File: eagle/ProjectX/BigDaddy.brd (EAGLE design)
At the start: 100 x 100 mm, 180 parts, among them U10 TC4427AEOA, U11 TC4427AEOA, U12 TC4427AEOA, U13 TC4427AEOA, U19 TC4427AEOA, U20 TC4427AEOA, U21 TC4427AEOA, U22 TC4427AEOA, U23 TC4427AEOA, U24 TC4427AEOA, U25 TC4427AEOA, U26 TC4427AEOA, U27 TC4427AEOA, U28 TC4427AEOA, U29 TC4427AEOA, U3 TC4427AEOA, U30 TC4427AEOA, U31 TC4427AEOA, U32 TC4427AEOA, U34 TC4427AEOA, U35 TC4427AEOA, U36 TC4427AEOA, U37 TC4427AEOA, U38 TC4427AEOA, U39 TC4427AEOA, U4 TC4427AEOA, U40 TC4427AEOA, U41 TC4427AEOA, U42 TC4427AEOA, U43 TC4427AEOA, U44 TC4427AEOA, U45 TC4427AEOA, U5 TC4427AEOA, U55 TC4427AEOA, U56 TC4427AEOA, U57 TC4427AEOA, U58 TC4427AEOA, U59 TC4427AEOA, U60 TC4427AEOA, U61 TC4427AEOA, U62 TC4427AEOA, U63 TC4427AEOA, U7 TC4427AEOA, U9 TC4427AEOA

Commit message: Still routing traces
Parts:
- J1: value (none) -> +20V
- J2: value (none) -> Data
- moved C19 0.25 mm to (7.25, 55.0)
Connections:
- net 23: now also DIP1.152
- net 24: now also DIP1.160
- net 25: now also DIP1.150
- net 30: now also DIP1.153
- net 31: now also DIP1.151
- net 34: now also DIP1.146
- net 39: now also DIP1.145
- net 40: now also DIP1.147
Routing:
- net 83: track 0.00 -> 47.1 mm
- net 82: track 0.00 -> 42.7 mm
- net 74: track 0.00 -> 41.0 mm
- net 73: track 0.00 -> 36.5 mm
- net 65: track 0.00 -> 35.2 mm
- net 64: track 0.00 -> 30.7 mm
- net 34: track 0.00 -> 30.0 mm, vias 0 -> 2
- net 56: track 0.00 -> 28.1 mm
- net 25: track 0.00 -> 27.2 mm, vias 0 -> 2
- net 30: track 0.00 -> 24.1 mm
- net 55: track 0.00 -> 23.5 mm
- net 31: track 0.00 -> 20.1 mm
- net 38: track 0.00 -> 19.9 mm
- net 47: track 0.00 -> 19.8 mm, vias 0 -> 2
- net 46: track 0.00 -> 16.8 mm, vias 0 -> 2
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
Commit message: About 80% complete routing
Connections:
- net 32: now also DIP1.139
- net 33: now also DIP1.144
- net 39: now also DIP1.147; no longer DIP1.145
- net 40: now also DIP1.145; no longer DIP1.147
- net 48: now also DIP1.140
- net 49: now also DIP1.138
- net 57: now also DIP1.135
- net 58: now also DIP1.133
- net 66: now also DIP1.129
- net 67: now also DIP1.127
- net 75: now also DIP1.123
- net 76: now also DIP1.120
- net 84: now also DIP1.116
- net 85: now also DIP1.113
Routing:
- net 84: track 0.00 -> 57.1 mm, vias 0 -> 2
- net 85: track 0.00 -> 54.1 mm, vias 0 -> 2
- net 75: track 0.00 -> 51.1 mm, vias 0 -> 2
- net 76: track 0.00 -> 48.1 mm, vias 0 -> 2
- net 66: track 0.00 -> 47.1 mm, vias 0 -> 2
- net 67: track 0.00 -> 44.2 mm, vias 0 -> 2
- net 57: track 0.00 -> 41.1 mm, vias 0 -> 2
- net 58: track 0.00 -> 38.1 mm, vias 0 -> 2
- net 48: track 0.00 -> 35.5 mm, vias 0 -> 2
- net 49: track 0.00 -> 32.4 mm, vias 0 -> 2
- net 39: track 0.00 -> 30.0 mm, vias 0 -> 2
- net 40: track 0.00 -> 26.8 mm, vias 0 -> 2
- net 33: track 0.00 -> 16.5 mm, vias 0 -> 2
- net 32: track 0.00 -> 12.1 mm, vias 0 -> 2
- net 34: track 30.0 -> 26.0 mm
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
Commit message: More work on routing
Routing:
- net 39: track 30.0 -> 29.2 mm

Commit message: Nearly done!
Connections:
- net 41: now also DIP1.122
- net 42: now also DIP1.126
- net 43: now also DIP1.119
- net 50: now also DIP1.108
- net 51: now also DIP1.112
- net 52: now also DIP1.115
- net 59: now also DIP1.100
- net 60: now also DIP1.106
- net 61: now also DIP1.98
- net 68: now also DIP1.90
- net 69: now also DIP1.93
- net 70: now also DIP1.96
- net 77: now also DIP1.97
- net 78: now also DIP1.94
- net 79: now also DIP1.99
- net 86: now also DIP1.109
- net 87: now also DIP1.107
- net 88: now also DIP1.102

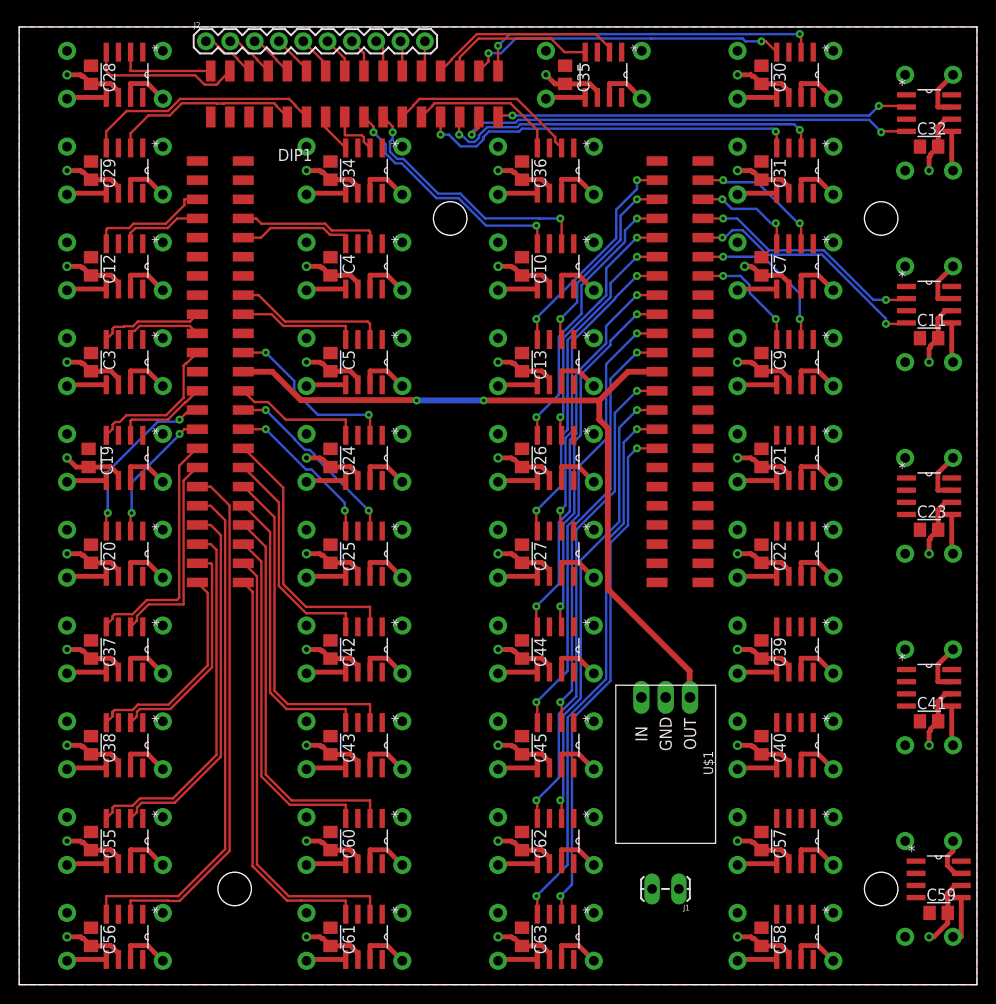
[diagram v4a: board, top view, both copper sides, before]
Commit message: Minor revision to add ground to the data port
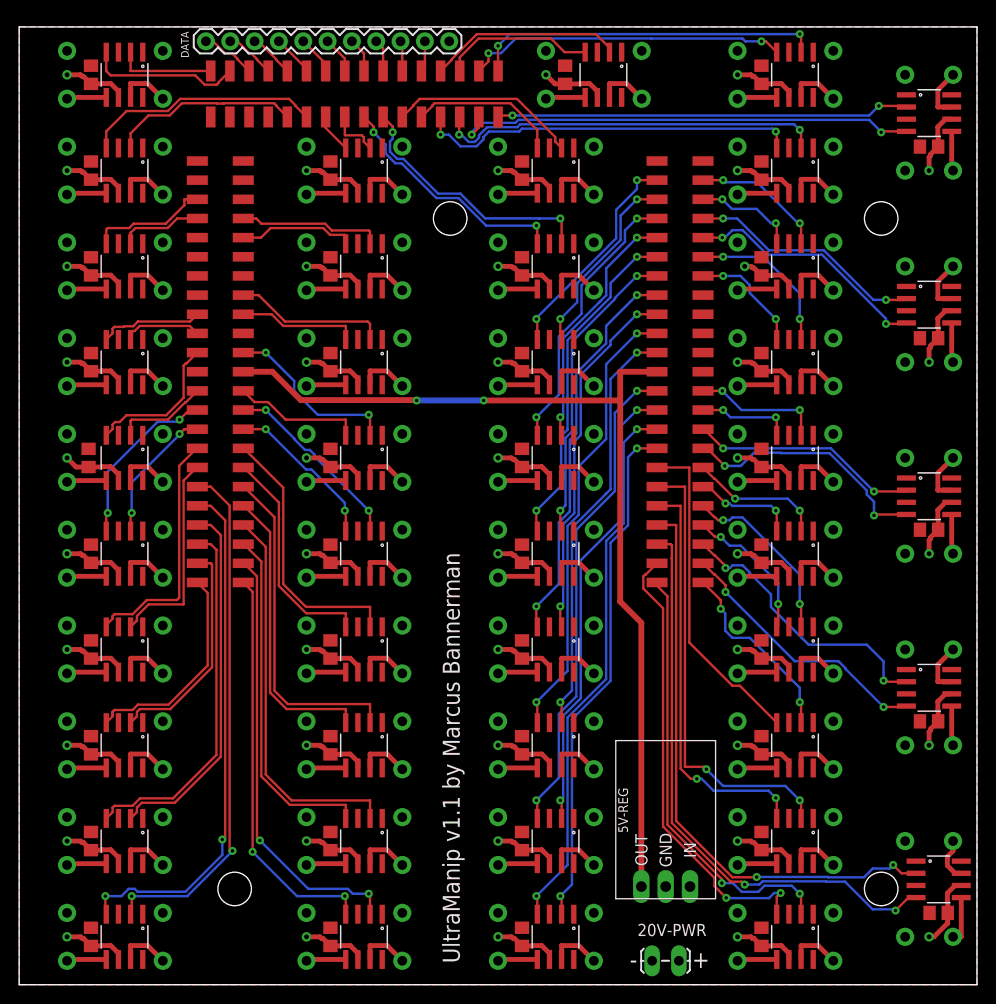
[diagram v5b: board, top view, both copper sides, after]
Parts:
- removed J1: +20V, SparkFun-Connectors:1X02_LOCK_LONGPADS
- removed J2: Data, SparkFun-Connectors:1X10
- removed U$1: OKI-78SR, Parts:OKI-78SR-HORIZ
- added 20V-PWR: +20V, SparkFun-Connectors:1X02_LOCK_LONGPADS
- added 5V-REG: OKI-78SR, Parts:OKI-78SR-HORIZ
- added DATA: Data, SparkFun-Connectors:1X11
- C10, C11, C12, C13, C19, C20, C21, C22, C23, C24, C25, C26, C27, C28, C29, C3, C30, C31, C32, C34, C35, C36, C37, C38, C39, C4, C40, C41, C42, C43, C44, C45, C5, C55, C56, C57, C58, C59, C60, C61, C62, C63, C7, C9: value (none) -> 100nF
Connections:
- net +5V: now also 5V-REG.OUT; no longer U$1.OUT
- net 68: now also DIP1.109; no longer DIP1.90
- net 77: now also DIP1.102; no longer DIP1.97
- net 78: now also DIP1.107; no longer DIP1.94
- net 86: now also DIP1.94; no longer DIP1.109
- net 87: now also DIP1.90; no longer DIP1.107
- net 88: now also DIP1.97; no longer DIP1.102
- net GND: now also 20V-PWR.2, 5V-REG.GND, DATA.11; no longer J1.2, U$1.GND
- net N$1: now also DATA.1; no longer J2.1
- net N$13: now also DATA.5; no longer J2.5
- net N$14: now also DATA.6; no longer J2.6
- net N$17: now also DATA.7; no longer J2.7
- net N$18: now also DATA.8; no longer J2.8
- net N$2: now also DATA.2; no longer J2.2
- net N$29: now also DATA.9; no longer J2.9
- net N$3: now also DATA.3; no longer J2.3
- net N$30: now also DATA.10; no longer J2.10
- net N$4: now also DATA.4; no longer J2.4
- net VDD: now also 20V-PWR.1, 5V-REG.IN; no longer J1.1, U$1.IN
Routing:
- net 79: track 0.00 -> 61.3 mm, vias 0 -> 2
- net 88: track 0.00 -> 60.7 mm, vias 0 -> 2
- net 78: track 0.00 -> 47.6 mm, vias 0 -> 2
- net 86: track 0.00 -> 47.4 mm, vias 0 -> 2
- net 87: track 0.00 -> 45.5 mm, vias 0 -> 2
- net 77: track 0.00 -> 43.3 mm, vias 0 -> 2
- net 68: track 0.00 -> 34.2 mm
- net 61: track 0.00 -> 29.5 mm, vias 0 -> 2
- net 70: track 0.00 -> 27.9 mm, vias 0 -> 2
- net 52: track 0.00 -> 26.6 mm, vias 0 -> 2
- net 43: track 0.00 -> 24.1 mm, vias 0 -> 2
- net 69: track 0.00 -> 19.9 mm, vias 0 -> 2
- net 60: track 0.00 -> 18.9 mm, vias 0 -> 2
- net +5V: track 80.6 -> 99.1 mm
- net 59: track 0.00 -> 15.0 mm, vias 0 -> 2
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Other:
- board text added: "+"
- board text added: "-"
- board text added: "UltraManip v1.1 by Marcus Bannerman"

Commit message: Slight improvements to the board, incase we need a new version in the future
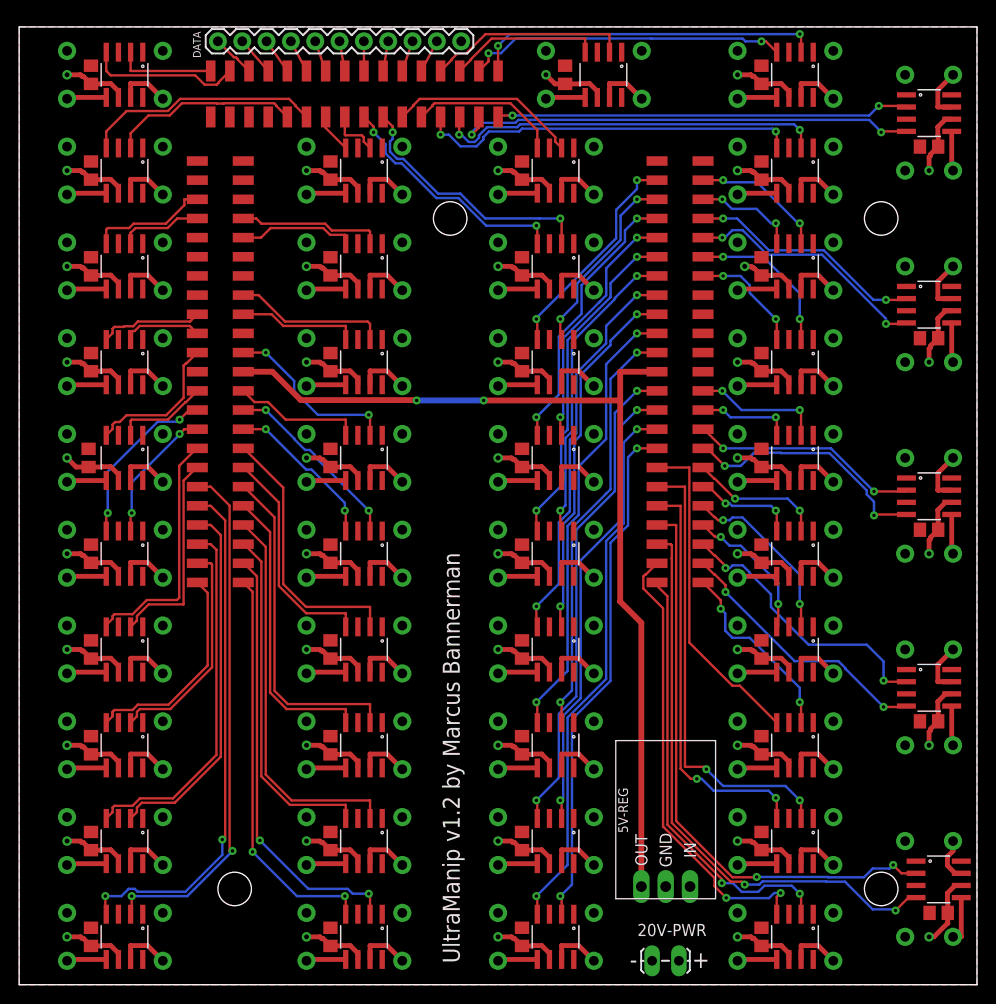
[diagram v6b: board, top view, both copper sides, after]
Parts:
- moved DATA 1.25 mm to (20.8, 98.5)
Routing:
- net N$1: track 5.82 -> 4.57 mm
- net N$2: track 5.28 -> 4.12 mm
- net N$3: track 4.74 -> 3.78 mm
- net 4: track 20.3 -> 21.2 mm
- net N$4: track 4.29 -> 3.50 mm
- net N$13: track 4.07 -> 3.29 mm
- net N$14: track 3.85 -> 3.15 mm
- net N$17: track 3.62 -> 3.10 mm
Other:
- board text added: "UltraManip v1.2 by Marcus Bannerman"
- board text removed: "UltraManip v1.1 by Marcus Bannerman"
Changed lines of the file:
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@@
 <hole x="90" y="80" drill="3.5"/>
 <hole x="45" y="80" drill="3.5"/>
-<text x="46" y="2.25" size="1.778" layer="21" rot="R90">UltraManip v1.1 by Marcus Bannerman</text>
-<text x="23.75" y="61" size="1.778" layer="22" rot="MR270">UltraManip v1.1 by Marcus Bannerman</text>
+<text x="46" y="2.25" size="1.778" layer="21" rot="R90">UltraManip v1.2 by Marcus Bannerman</text>
+<text x="23.75" y="61" size="1.778" layer="22" rot="MR270">UltraManip v1.2 by Marcus Bannerman</text>
 <text x="70.25" y="1.75" size="1.778" layer="21">+</text>
 <text x="63.75" y="1.75" size="1.778" layer="21">-</text>
@@
 </element>
 <element name="5V-REG" library="Parts" package="OKI-78SR-HORIZ" value="OKI-78SR" x="67.5" y="10.25"/>
-<element name="DATA" library="SparkFun-Connectors" library_urn="urn:adsk.eagle:library:513" package="1X11" package3d_urn="urn:adsk.eagle:package:38251/1" value="Data" x="19.5" y="98.5" smashed="yes">
-<attribute name="NAME" x="16.897" y="99.52" size="0.8128" layer="25" font="vector" ratio="20" rot="R270"/>
-<attribute name="VALUE" x="18.23" y="96.468" size="0.6096" layer="27" font="vector" ratio="20"/>
+<element name="DATA" library="SparkFun-Connectors" library_urn="urn:adsk.eagle:library:513" package="1X11" package3d_urn="urn:adsk.eagle:package:38251/1" value="Data" x="20.75" y="98.5" smashed="yes">
+<attribute name="NAME" x="18.147" y="99.52" size="0.8128" layer="25" font="vector" ratio="20" rot="R270"/>
 </element>
 </elements>
@@
 <contactref element="5V-REG" pad="GND"/>
 <contactref element="DATA" pad="11"/>
+<wire x1="55" y1="97.5" x2="46.15" y2="98.5" width="0" layer="19" extent="1-1"/>
 </signal>
 <signal name="VDD">
@@
 <contactref element="DATA" pad="1"/>
 <contactref element="DIP1" pad="203"/>
+<wire x1="22.8302" y1="96.636775" x2="22.636775" y2="96.8302" width="0.254" layer="1"/>
+<wire x1="22.636775" y1="96.8302" x2="22.4198" y2="96.8302" width="0.254" layer="1"/>
+<wire x1="22.4198" y1="96.8302" x2="20.75" y2="98.5" width="0.254" layer="1"/>
 <wire x1="24" y1="95.4" x2="22.8302" y2="96.5698" width="0.254" layer="1"/>
 <wire x1="22.8302" y1="96.5698" x2="22.8302" y2="96.636775" width="0.254" layer="1"/>
-<wire x1="20.24394375" y1="98.5" x2="19.5" y2="98.5" width="0.254" layer="1"/>
-<wire x1="21.51394375" y1="97.23" x2="20.24394375" y2="98.5" width="0.254" layer="1"/>
-<wire x1="22.8302" y1="96.636775" x2="22.236975" y2="97.23" width="0.254" layer="1"/>
-<wire x1="22.236975" y1="97.23" x2="21.51394375" y2="97.23" width="0.254" layer="1"/>
 </signal>
 <signal name="N$2">
 <contactref element="DATA" pad="2"/>
 <contactref element="DIP1" pad="200"/>
-<wire x1="26" y1="95.4" x2="24.8302" y2="96.5698" width="0.254" layer="1"/>
-<wire x1="24.8302" y1="96.5698" x2="24.8302" y2="96.636775" width="0.254" layer="1"/>
-<wire x1="22.78394375" y1="98.5" x2="22.04" y2="98.5" width="0.254" layer="1"/>
-<wire x1="24.05394375" y1="97.23" x2="22.78394375" y2="98.5" width="0.254" layer="1"/>
-<wire x1="24.8302" y1="96.636775" x2="24.236975" y2="97.23" width="0.254" layer="1"/>
-<wire x1="24.236975" y1="97.23" x2="24.05394375" y2="97.23" width="0.254" layer="1"/>
+<wire x1="26" y1="95.4" x2="23.29" y2="98.5" width="0.254" layer="1"/>
 </signal>
 <signal name="N$3">
 <contactref element="DATA" pad="3"/>
 <contactref element="DIP1" pad="197"/>
-<wire x1="28" y1="95.4" x2="26.8302" y2="96.5698" width="0.254" layer="1"/>
-<wire x1="26.8302" y1="96.5698" x2="26.8302" y2="96.636775" width="0.254" layer="1"/>
-<wire x1="26.8302" y1="96.636775" x2="24.966975" y2="98.5" width="0.254" layer="1"/>
-<wire x1="24.966975" y1="98.5" x2="24.58" y2="98.5" width="0.254" layer="1"/>
+<wire x1="28" y1="95.4" x2="25.83" y2="98.5" width="0.254" layer="1"/>
 </signal>
 <signal name="N$4">
 <contactref element="DATA" pad="4"/>
 <contactref element="DIP1" pad="193"/>
-<wire x1="30" y1="95.4" x2="30" y2="95.62" width="0.254" layer="1"/>
-<wire x1="30" y1="95.62" x2="27.12" y2="98.5" width="0.254" layer="1"/>
+<wire x1="30" y1="95.4" x2="28.37" y2="98.5" width="0.254" layer="1"/>
 </signal>
 <signal name="N$13">
 <contactref element="DATA" pad="5"/>
 <contactref element="DIP1" pad="190"/>
-<wire x1="32" y1="95.4" x2="32" y2="96.16" width="0.254" layer="1"/>
-<wire x1="32" y1="96.16" x2="29.66" y2="98.5" width="0.254" layer="1"/>
+<wire x1="32" y1="95.4" x2="30.91" y2="98.5" width="0.254" layer="1"/>
 </signal>
 <signal name="N$14">
 <contactref element="DATA" pad="6"/>
 <contactref element="DIP1" pad="187"/>
-<wire x1="34" y1="95.4" x2="34" y2="96.7" width="0.254" layer="1"/>
-<wire x1="34" y1="96.7" x2="32.2" y2="98.5" width="0.254" layer="1"/>
+<wire x1="34" y1="95.4" x2="33.45" y2="98.5" width="0.254" layer="1"/>
 </signal>
 <signal name="N$17">
 <contactref element="DATA" pad="7"/>
 <contactref element="DIP1" pad="185"/>
-<wire x1="36" y1="95.4" x2="36" y2="97.24" width="0.254" layer="1"/>
-<wire x1="36" y1="97.24" x2="34.74" y2="98.5" width="0.254" layer="1"/>
+<wire x1="36" y1="95.4" x2="35.99" y2="98.5" width="0.254" layer="1"/>
 </signal>
 <signal name="N$18">
 <contactref element="DATA" pad="8"/>
 <contactref element="DIP1" pad="180"/>
-<wire x1="38" y1="95.4" x2="38" y2="97.78" width="0.254" layer="1"/>
-<wire x1="38" y1="97.78" x2="37.28" y2="98.5" width="0.254" layer="1"/>
+<wire x1="38" y1="95.4" x2="38.53" y2="98.5" width="0.254" layer="1"/>
 </signal>
 <signal name="N$29">
 <contactref element="DATA" pad="9"/>
 <contactref element="DIP1" pad="178"/>
-<wire x1="40" y1="95.4" x2="40" y2="98.32" width="0.254" layer="1"/>
-<wire x1="40" y1="98.32" x2="39.82" y2="98.5" width="0.254" layer="1"/>
+<wire x1="40" y1="95.4" x2="41.07" y2="98.5" width="0.254" layer="1"/>
 </signal>
 <signal name="N$30">
 <contactref element="DATA" pad="10"/>
 <contactref element="DIP1" pad="172"/>
-<wire x1="42" y1="95.4" x2="42.36" y2="95.76" width="0.254" layer="1"/>
-<wire x1="42.36" y1="95.76" x2="42.36" y2="98.5" width="0.254" layer="1"/>
+<wire x1="42" y1="95.4" x2="43.61" y2="98.5" width="0.254" layer="1"/>
 </signal>
 <signal name="1">
@@
 <contactref element="DIP1" pad="165"/>
 <contactref element="U35" pad="4"/>
-<wire x1="56.9518125" y1="97.3622" x2="59.095" y2="97.3622" width="0.254" layer="1"/>
-<wire x1="55.5313125" y1="98.7827" x2="56.9518125" y2="97.3622" width="0.254" layer="1"/>
-<wire x1="46" y1="95.4" x2="46" y2="96.82039375" width="0.254" layer="1"/>
-<wire x1="46" y1="96.82039375" x2="47.96230625" y2="98.7827" width="0.254" layer="1"/>
-<wire x1="47.96230625" y1="98.7827" x2="55.5313125" y2="98.7827" width="0.254" layer="1"/>
+<wire x1="46" y1="95.4" x2="47.1698" y2="96.5698" width="0.254" layer="1"/>
+<wire x1="47.1698" y1="96.5698" x2="47.1698" y2="96.636775" width="0.254" layer="1"/>
+<wire x1="47.1698" y1="96.636775" x2="49.315725" y2="98.7827" width="0.254" layer="1"/>
+<wire x1="49.315725" y1="98.7827" x2="59.095" y2="98.7827" width="0.254" layer="1"/>
+<wire x1="59.095" y1="98.7827" x2="59.095" y2="97.3622" width="0.254" layer="1"/>
 </signal>
 <signal name="4">
 <contactref element="DIP1" pad="168"/>
 <contactref element="U35" pad="2"/>
-<wire x1="61.464175" y1="98" x2="61.5" y2="98" width="0.254" layer="1"/>
-<wire x1="45.1698" y1="96.636775" x2="47.772925" y2="99.2399" width="0.254" layer="1"/>
+<wire x1="61.5" y1="98" x2="61.464175" y2="98" width="0.254" layer="1"/>
 <wire x1="44" y1="95.4" x2="45.1698" y2="96.5698" width="0.254" layer="1"/>
 <wire x1="45.1698" y1="96.5698" x2="45.1698" y2="96.636775" width="0.254" layer="1"/>
-<wire x1="47.772925" y1="99.2399" x2="60.224275" y2="99.2399" width="0.254" layer="1"/>
-<wire x1="60.224275" y1="99.2399" x2="61.464175" y2="98" width="0.254" layer="1"/>
-<wire x1="61.5" y1="98" x2="61.635" y2="97.865" width="0.254" layer="1"/>
-<wire x1="61.635" y1="97.865" x2="61.635" y2="97.3622" width="0.254" layer="1"/>
+<wire x1="46.67605625" y1="97.23" x2="48.68595625" y2="99.2399" width="0.254" layer="1"/>
+<wire x1="45.1698" y1="96.636775" x2="45.763025" y2="97.23" width="0.254" layer="1"/>
+<wire x1="45.763025" y1="97.23" x2="46.67605625" y2="97.23" width="0.254" layer="1"/>
+<wire x1="61.635" y1="99.2399" x2="61.635" y2="97.3622" width="0.254" layer="1"/>
+<wire x1="48.68595625" y1="99.2399" x2="61.635" y2="99.2399" width="0.254" layer="1"/>
+<wire x1="61.635" y1="97.3622" x2="61.5" y2="98" width="0" layer="19" extent="1-1"/>
 </signal>
 <signal name="5">
